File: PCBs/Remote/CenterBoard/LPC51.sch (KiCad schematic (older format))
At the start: 24 parts, among them J201 DX07S016JA1R1500, U201 LPC51U68JBD64, U202 W25Q128JVS

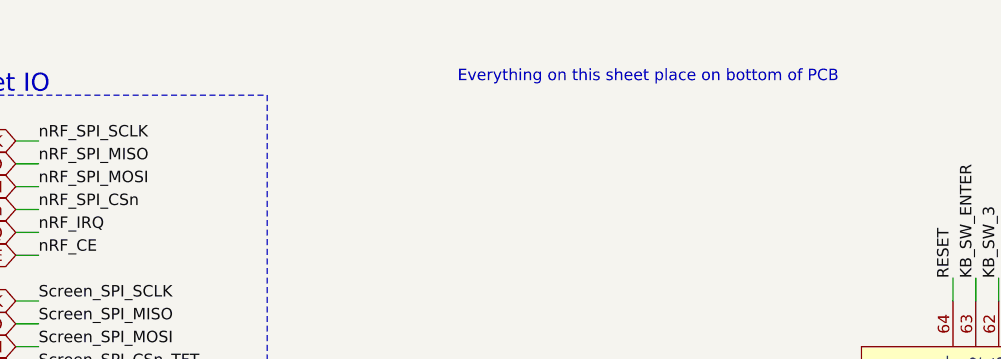
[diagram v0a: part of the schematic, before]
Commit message: Some cleanup, and PCB antenna removal.
Last edits before asking for reddit feedback.

Signed-off-by: Eldalote.Electronics <Eldalote.Electronics@gmail.com>
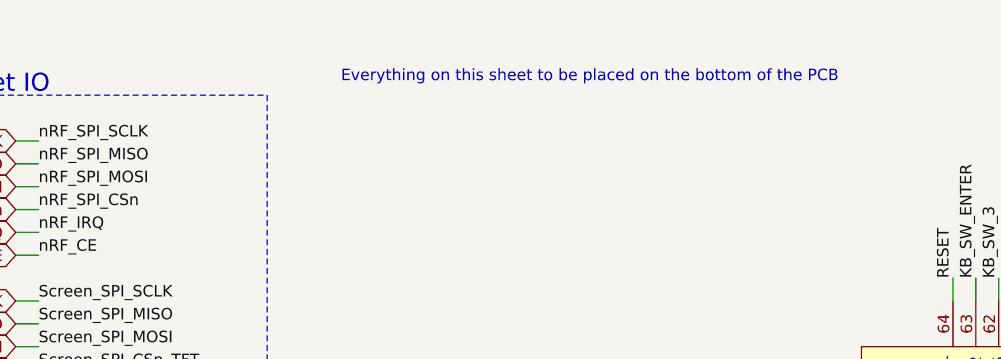
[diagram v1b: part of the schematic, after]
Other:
- note added: "Everything on this sheet to be placed on the bottom of the PCB"
- note removed: "Everything on this sheet place on bottom of PCB"
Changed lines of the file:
@@
 Sheet IO
 Text Notes 5100 750  2    50   ~ 0
-Everything on this sheet place on bottom of PCB
+Everything on this sheet to be placed on the bottom of the PCB
 $EndSCHEMATC
